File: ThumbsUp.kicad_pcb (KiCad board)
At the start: 2 copper layers, 251.1 x 336.1 mm, 135 parts, among them J1 Conn_01x04_Male, J10 Raiser_Male, J11 Raiser_Female, J12 Raiser_Male, J13 Raiser_Female, J14 Raiser_Male, J15 Raiser_Female, J16 Raiser_Male, J17 Raiser_Female, J18 Raiser_Male, J2 Conn_01x04_Male, J20 Conn_01x04_Female, J21 Conn_01x04_Female, J22 Conn_01x04_Female, J23 Conn_01x04_Female, J24 Conn_01x04_Male, J25 Conn_01x04_Male, J26 Conn_01x04_Male, J27 Conn_01x04_Male, J28 Conn_01x04_Female, J29 Conn_01x04_Female, J3 Conn_01x04_Female, J30 Conn_01x04_Female, J31 Conn_01x04_Female, J4 Conn_01x04_Male, J5 Conn_01x04_Female, J6 Conn_01x04_Male, J7 Conn_01x04_Male, J8 Conn_01x04_Male, J9 Raiser_Female, U1 ATmega32U4-AU, Y1 16MHz

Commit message: End of the day resuls
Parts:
- added J26: Conn_01x04_Male, Connector_PinHeader_2.54mm:PinHeader_1x04_P2.54mm_Vertical, F.Cu at (180.6, 164.0)
- added J27: Conn_01x04_Male, Connector_PinHeader_2.54mm:PinHeader_1x04_P2.54mm_Vertical, F.Cu at (187.1, 180.5)
- added J30: Conn_01x04_Female, Connector_PinSocket_2.54mm:PinSocket_1x04_P2.54mm_Vertical, F.Cu at (178.9, 301.4)
- added J31: Conn_01x04_Female, Connector_PinSocket_2.54mm:PinSocket_1x04_P2.54mm_Vertical, F.Cu at (185.4, 317.9)
- C1, C10, C2, C3, C4, C5, C6, C7, C8, C9, D1, D10, D11, D12, D13, D14, D15, D16, D17, D18, D19, D2, D20, D21, D22, D23, D24, D25, D26, D27, D28, D29, D3, D30, D31, D32, D33, D34, D35, D36, D37, D38, D39, D4, D40, D41, D42, D43, D44, D5, D6, D7, D8, D9, F1, R1, R2, R3, R4, U1, Y1: moved to B.Cu
- moved C5 38.6 mm to (177.7, -35.2)
- moved D14 33.1 mm to (179.0, 0.65)
- moved D20 33.1 mm to (173.3, 0.65)
- moved C9 32.7 mm to (177.7, -32.2)
- moved D12 30.7 mm to (192.4, -31.2)
- moved D23 29.0 mm to (37.9, -30.4)
- moved D24 29.0 mm to (49.4, -30.4)
- moved D25 29.0 mm to (55.1, -30.4)
- moved D32 29.0 mm to (124.1, -30.4)
- moved D33 29.0 mm to (118.4, -30.4)
- moved D34 29.0 mm to (112.6, -30.4)
- moved D35 29.0 mm to (106.9, -30.4)
- moved D36 29.0 mm to (101.1, -30.4)
- moved D37 29.0 mm to (43.6, -30.4)
- moved D38 29.0 mm to (95.4, -30.4)
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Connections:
- J10 pad 1: (no net) -> Net-(J10-Pad1)
- J10 pad 2: (no net) -> Net-(J10-Pad2)
- J10 pad 3: (no net) -> Net-(J10-Pad3)
- J10 pad 4: (no net) -> Net-(J10-Pad4)
- J11 pad 1: (no net) -> Net-(J11-Pad1)
- J11 pad 2: (no net) -> Net-(J11-Pad2)
- J11 pad 3: (no net) -> Net-(J11-Pad3)
- J11 pad 4: (no net) -> Net-(J11-Pad4)
- J13 pad 1: (no net) -> Net-(J13-Pad1)
- J13 pad 2: (no net) -> Net-(J13-Pad2)
- J13 pad 3: (no net) -> Net-(J13-Pad3)
- J13 pad 4: (no net) -> Net-(J13-Pad4)
- J14 pad 1: (no net) -> Net-(J14-Pad1)
- J14 pad 2: (no net) -> Net-(J14-Pad2)
- J14 pad 3: (no net) -> Net-(J14-Pad3)
- J14 pad 4: (no net) -> Net-(J14-Pad4)
- J15 pad 1: (no net) -> Net-(J15-Pad1)
- J15 pad 2: (no net) -> Net-(J15-Pad2)
- J15 pad 3: (no net) -> Net-(J15-Pad3)
- J15 pad 4: (no net) -> Net-(J15-Pad4)
- J17 pad 1: (no net) -> VCC
- J17 pad 2: (no net) -> SDA
- J17 pad 3: (no net) -> SCL
- J17 pad 4: (no net) -> GND
- J18 pad 1: (no net) -> VCC
- J18 pad 2: (no net) -> SDA
- J18 pad 3: (no net) -> SCL
- J18 pad 4: (no net) -> GND
- J20 pad 1: (no net) -> COL3
- J20 pad 2: (no net) -> COL2
- J20 pad 3: (no net) -> COL1
- J20 pad 4: (no net) -> COL0
- J21 pad 1: (no net) -> Net-(D4-Pad2)
- J21 pad 2: (no net) -> Net-(D3-Pad2)
- J21 pad 3: (no net) -> Net-(D2-Pad2)
- J21 pad 4: (no net) -> Net-(D1-Pad2)
- J22 pad 1: (no net) -> Net-(D8-Pad2)
- J22 pad 2: (no net) -> Net-(D7-Pad2)
- J22 pad 3: (no net) -> Net-(D6-Pad2)
- J22 pad 4: (no net) -> Net-(D5-Pad2)
- J23 pad 1: (no net) -> Net-(D12-Pad2)
- J23 pad 2: (no net) -> Net-(D11-Pad2)
- J23 pad 3: (no net) -> Net-(D10-Pad2)
- J23 pad 4: (no net) -> Net-(D9-Pad2)
- J24 pad 1: (no net) -> COL8
- J24 pad 2: (no net) -> COL9
- J24 pad 3: (no net) -> COLA
- J24 pad 4: (no net) -> COLB
- J25 pad 1: (no net) -> Net-(D34-Pad2)
- J25 pad 2: (no net) -> Net-(D33-Pad2)
- J25 pad 3: (no net) -> Net-(D32-Pad2)
- J25 pad 4: (no net) -> Net-(D31-Pad2)
- J26 pad 1: (no net) -> Net-(D38-Pad2)
- J26 pad 2: (no net) -> Net-(D37-Pad2)
- J26 pad 3: (no net) -> Net-(D36-Pad2)
- J26 pad 4: (no net) -> Net-(D35-Pad2)
- J27 pad 1: (no net) -> Net-(D42-Pad2)
- J27 pad 2: (no net) -> Net-(D41-Pad2)
- J27 pad 3: (no net) -> Net-(D40-Pad2)
- J27 pad 4: (no net) -> Net-(D39-Pad2)
- J3 pad 1: (no net) -> Net-(J3-Pad1)
- J3 pad 2: (no net) -> Net-(J3-Pad2)
- J3 pad 3: (no net) -> Net-(J3-Pad3)
- J3 pad 4: (no net) -> Net-(J3-Pad4)
- J4 pad 1: (no net) -> COL4
- J4 pad 2: (no net) -> Net-(D18-Pad2)
- J4 pad 3: (no net) -> Net-(D19-Pad2)
- J4 pad 4: (no net) -> COL5
- J5 pad 1: (no net) -> Net-(J5-Pad1)
- J5 pad 2: (no net) -> Net-(J5-Pad2)
- J5 pad 3: (no net) -> Net-(J5-Pad3)
- J5 pad 4: (no net) -> Net-(J5-Pad4)
- J6 pad 1: (no net) -> COL6
- J6 pad 2: (no net) -> Net-(D29-Pad2)
- J6 pad 3: (no net) -> Net-(D30-Pad2)
- J6 pad 4: (no net) -> COL7
- J9 pad 1: (no net) -> Net-(J9-Pad1)
- J9 pad 2: (no net) -> Net-(J9-Pad2)
- J9 pad 3: (no net) -> Net-(J9-Pad3)
- J9 pad 4: (no net) -> Net-(J9-Pad4)
- MX1 pad 1: Net-(MX1-Pad1) -> Net-(J1-Pad4)
- MX10 pad 1: (no net) -> COL2
- MX10 pad 2: (no net) -> Net-(D14-Pad2)
- MX11 pad 1: Net-(MX11-Pad1) -> Net-(J1-Pad1)
- MX12 pad 1: Net-(MX12-Pad1) -> Net-(J1-Pad1)
- MX14 pad 1: (no net) -> COL3
- MX14 pad 2: (no net) -> Net-(D13-Pad2)
- MX15 pad 1: (no net) -> Net-(MX15-Pad1)
- MX15 pad 2: (no net) -> Net-(D15-Pad2)
- MX16 pad 1: (no net) -> Net-(MX16-Pad1)
- MX16 pad 2: (no net) -> Net-(D16-Pad2)
- MX17 pad 1: (no net) -> Net-(MX17-Pad1)
- MX17 pad 2: (no net) -> Net-(D17-Pad2)
- MX18 pad 1: (no net) -> Net-(J3-Pad1)
- MX18 pad 2: (no net) -> Net-(J3-Pad2)
- MX19 pad 1: (no net) -> Net-(MX19-Pad1)
- MX19 pad 2: (no net) -> Net-(D20-Pad2)
- MX2 pad 1: Net-(MX2-Pad1) -> Net-(J1-Pad4)
- MX20 pad 1: (no net) -> Net-(MX20-Pad1)
- MX20 pad 2: (no net) -> Net-(D21-Pad2)
- MX21 pad 1: (no net) -> Net-(MX21-Pad1)
- MX21 pad 2: (no net) -> Net-(D22-Pad2)
- MX22 pad 1: (no net) -> Net-(J3-Pad4)
- MX22 pad 2: (no net) -> Net-(J3-Pad3)
- MX23 pad 1: (no net) -> Net-(MX23-Pad1)
- MX23 pad 2: (no net) -> Net-(D23-Pad2)
- MX24 pad 1: (no net) -> Net-(MX24-Pad1)
- MX24 pad 2: (no net) -> Net-(D24-Pad2)
- MX25 pad 1: (no net) -> Net-(MX25-Pad1)
- MX25 pad 2: (no net) -> Net-(D25-Pad2)
- MX26 pad 1: (no net) -> Net-(J5-Pad1)
- MX26 pad 2: (no net) -> Net-(J5-Pad2)
- MX27 pad 1: (no net) -> Net-(MX27-Pad1)
- MX27 pad 2: (no net) -> Net-(D26-Pad2)
- MX28 pad 1: (no net) -> Net-(MX28-Pad1)
- MX28 pad 2: (no net) -> Net-(D27-Pad2)
- MX29 pad 1: (no net) -> Net-(MX29-Pad1)
- MX29 pad 2: (no net) -> Net-(D28-Pad2)
- MX30 pad 1: (no net) -> Net-(J5-Pad4)
- MX30 pad 2: (no net) -> Net-(J5-Pad3)
- MX34 pad 1: (no net) -> COL8
- MX34 pad 2: (no net) -> Net-(D43-Pad2)
- MX38 pad 1: (no net) -> COL9
- MX38 pad 2: (no net) -> Net-(D44-Pad2)
- MX39 pad 1: Net-(MX39-Pad1) -> Net-(J28-Pad3)
- MX4 pad 1: Net-(MX4-Pad1) -> Net-(J1-Pad3)
- MX40 pad 1: Net-(MX40-Pad1) -> Net-(J28-Pad3)
- MX42 pad 1: Net-(MX42-Pad1) -> Net-(J28-Pad4)
- MX43 pad 1: Net-(MX43-Pad1) -> Net-(J28-Pad4)
- MX5 pad 1: Net-(MX5-Pad1) -> Net-(J1-Pad3)
- MX7 pad 1: Net-(MX7-Pad1) -> Net-(J1-Pad2)
- MX8 pad 1: Net-(MX8-Pad1) -> Net-(J1-Pad2)
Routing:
- net Net-(J28-Pad4): track 0.00 -> 123.3 mm
- net Net-(J1-Pad4): track 0.00 -> 119.0 mm, vias 0 -> 1
- net Net-(J28-Pad1): track 0.00 -> 109.6 mm, vias 0 -> 2
- net Net-(J8-Pad1): track 0.00 -> 108.3 mm
- net Net-(J7-Pad1): track 0.00 -> 107.5 mm
- net Net-(J1-Pad1): track 0.00 -> 106.8 mm
- net Net-(J30-Pad1): track 0.00 -> 104.9 mm
- net Net-(J1-Pad3): track 0.00 -> 104.5 mm, vias 0 -> 1
- net Net-(J29-Pad1): track 0.00 -> 100.3 mm
- net Net-(J28-Pad3): track 0.00 -> 97.1 mm, vias 0 -> 2
- net Net-(J1-Pad2): track 0.00 -> 96.2 mm
- net Net-(J31-Pad1): track 0.00 -> 96.2 mm
- net Net-(J2-Pad1): track 0.00 -> 94.8 mm
- net Net-(J28-Pad2): track 0.00 -> 90.4 mm, vias 0 -> 2
- net Net-(J2-Pad2): track 0.00 -> 82.4 mm
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
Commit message: End of the day resuls
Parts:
- moved U1 234.1 mm to (146.6, 220.0)
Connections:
- MX15 pad 1: Net-(MX15-Pad1) -> COL4
- MX16 pad 1: Net-(MX16-Pad1) -> COL4
- MX17 pad 1: Net-(MX17-Pad1) -> COL4
- MX19 pad 1: Net-(MX19-Pad1) -> COL5
- MX20 pad 1: Net-(MX20-Pad1) -> COL5
- MX21 pad 1: Net-(MX21-Pad1) -> COL5
- MX23 pad 1: Net-(MX23-Pad1) -> COL6
- MX24 pad 1: Net-(MX24-Pad1) -> COL6
- MX25 pad 1: Net-(MX25-Pad1) -> COL6
- MX27 pad 1: Net-(MX27-Pad1) -> COL7
- MX28 pad 1: Net-(MX28-Pad1) -> COL7
- MX29 pad 1: Net-(MX29-Pad1) -> COL7
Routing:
- net COL7: track 0.00 -> 62.8 mm, vias 0 -> 3
- net COL4: track 0.00 -> 61.7 mm, vias 0 -> 3
- net COL6: track 0.00 -> 60.6 mm, vias 0 -> 3
- net COL5: track 0.00 -> 59.2 mm, vias 0 -> 4
- net COL9: track 0.00 -> 13.2 mm, vias 0 -> 1
- net COL8: track 0.00 -> 12.9 mm, vias 0 -> 1
- net Net-(J1-Pad4): track 119.0 -> 130.2 mm
- net Net-(J29-Pad1): track 100.3 -> 110.0 mm
- net Net-(J30-Pad1): track 104.9 -> 112.9 mm
- net Net-(J28-Pad1): track 109.6 -> 115.7 mm
- net Net-(J29-Pad3): track 51.9 -> 57.8 mm
- net Net-(J28-Pad3): track 97.1 -> 102.7 mm
- net Net-(J8-Pad2): track 74.7 -> 80.3 mm
- net Net-(J28-Pad2): track 90.4 -> 95.0 mm
- net Net-(J8-Pad1): track 108.3 -> 104.5 mm
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
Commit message: Laid some tracks
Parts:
- added SW1: SW_Push, random-keyboard-parts:SKQG-1155865, B.Cu at (164.7, 227.9)
- added USB1: Molex-0548190589, random-keyboard-parts:Molex-0548190589, B.Cu at (146.7, 155.0)
- moved R4 275.0 mm to (158.8, 221.9), turned to 180 degrees
- moved D44 273.2 mm to (194.5, 208.0), turned to 90 degrees
- moved D43 269.4 mm to (192.1, 208.0), turned to 90 degrees
- moved D25 268.1 mm to (177.8, 208.0), turned to 90 degrees
- moved C9 262.9 mm to (128.0, 225.9)
- moved D42 261.6 mm to (180.2, 208.0), turned to 90 degrees
- moved D41 260.2 mm to (182.6, 208.0), turned to 90 degrees
- moved C6 259.0 mm to (131.5, 221.6)
- moved D40 258.9 mm to (184.9, 208.0), turned to 90 degrees
- moved D39 257.6 mm to (187.3, 208.0), turned to 90 degrees
- moved C10 254.2 mm to (124.8, 220.7)
- moved D12 251.2 mm to (115.9, 208.0), turned to 90 degrees
- moved C7 251.1 mm to (131.2, 216.0)
- moved C1 249.1 mm to (129.8, 218.8)
- moved D19 248.7 mm to (96.8, 208.0), turned to 90 degrees
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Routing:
- net Net-(D27-Pad2): track 0.00 -> 70.5 mm, vias 0 -> 1
- net Net-(D26-Pad2): track 0.00 -> 69.3 mm, vias 0 -> 1
- net Net-(D15-Pad2): track 0.00 -> 65.0 mm, vias 0 -> 1
- net Net-(D16-Pad2): track 0.00 -> 64.6 mm, vias 0 -> 1
- net Net-(D14-Pad2): track 0.00 -> 62.7 mm, vias 0 -> 2
- net COL5: track 59.2 -> 119.7 mm, vias 4 -> 1
- net Net-(D44-Pad2): track 0.00 -> 59.6 mm
- net COL6: track 60.6 -> 113.0 mm, vias 3 -> 2
- net Net-(D5-Pad2): track 0.00 -> 52.4 mm, vias 0 -> 1
- net Net-(D6-Pad2): track 0.00 -> 51.2 mm, vias 0 -> 1
- net COL7: track 62.8 -> 110.8 mm, vias 3 -> 1
- net Net-(J5-Pad3): track 0.00 -> 47.7 mm
- net Net-(D35-Pad2): track 0.00 -> 47.7 mm, vias 0 -> 1
- net Net-(D28-Pad2): track 0.00 -> 47.2 mm, vias 0 -> 1
- net COL3: track 0.00 -> 46.8 mm
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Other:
- net class Power added: clearance 0.2, trace_width 0.381, via_dia 0.8, via_drill 0.4

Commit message: Tracks are almost finished
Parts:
- moved C9 35.3 mm to (146.8, 196.1)
- moved C2 31.0 mm to (155.7, 207.8)
- moved C8 30.4 mm to (146.8, 199.2)
- moved C3 28.5 mm to (146.8, 201.6)
- moved C1 19.1 mm to (138.0, 201.6), turned to 180 degrees
- moved R4 18.3 mm to (140.5, 221.6), turned to 90 degrees
- moved C10 18.1 mm to (134.9, 205.6), turned to 270 degrees
- moved C7 17.4 mm to (147.6, 221.5), turned to 270 degrees
- moved C6 7.30 mm to (134.9, 215.1), turned to 90 degrees
- moved R3 6.95 mm to (151.6, 221.3)
- moved U1 5.18 mm to (144.5, 210.5)
- moved C4 2.86 mm to (165.9, 213.5)
- moved C5 2.86 mm to (165.9, 208.9)
- moved Y1 2.86 mm to (161.6, 211.3)
- moved F1 1.60 mm to (141.3, 188.9)
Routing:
- net ROW3: track 0.00 -> 126.8 mm
- net VCC: track 2.76 -> 118.6 mm, vias 0 -> 5
- net COLA: track 0.00 -> 115.8 mm, vias 0 -> 1
- net COLB: track 0.00 -> 115.4 mm, vias 0 -> 1
- net COL2: track 19.6 -> 125.6 mm, vias 1 -> 4
- net COL9: track 25.2 -> 130.8 mm, vias 0 -> 1
- net COL0: track 0.00 -> 104.7 mm, vias 0 -> 1
- net COL1: track 0.00 -> 104.6 mm, vias 0 -> 1
- net ROW2: track 2.32 -> 105.7 mm, vias 0 -> 2
- net COL8: track 45.6 -> 145.9 mm, vias 0 -> 1
- net COL7: track 110.8 -> 209.9 mm, vias 1 -> 3
- net COL3: track 46.8 -> 127.8 mm, vias 0 -> 3
- net GND: track 33.8 -> 114.3 mm, vias 0 -> 5
- net COL6: track 113.0 -> 177.7 mm, vias 2 -> 4
- net COL4: track 105.1 -> 168.7 mm, vias 0 -> 1
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- added copper zone on B.Cu, net GND

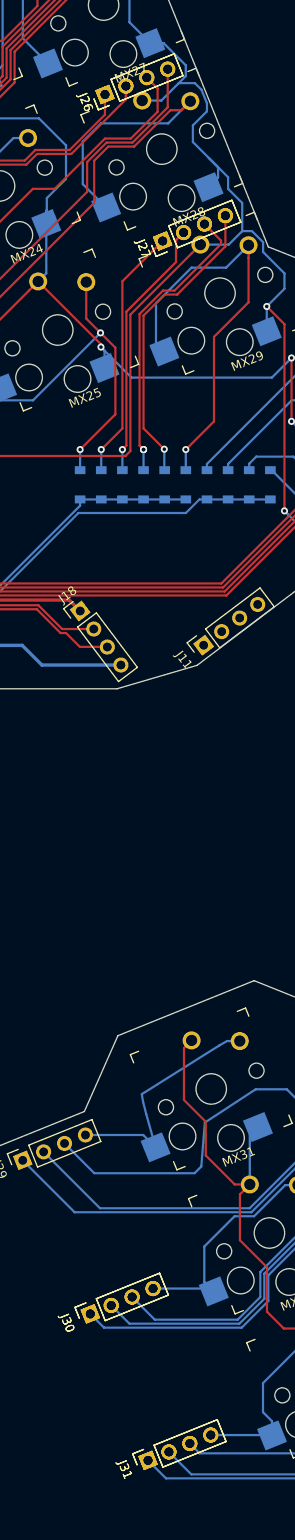
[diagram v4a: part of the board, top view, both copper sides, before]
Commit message: Removed the exta footprints
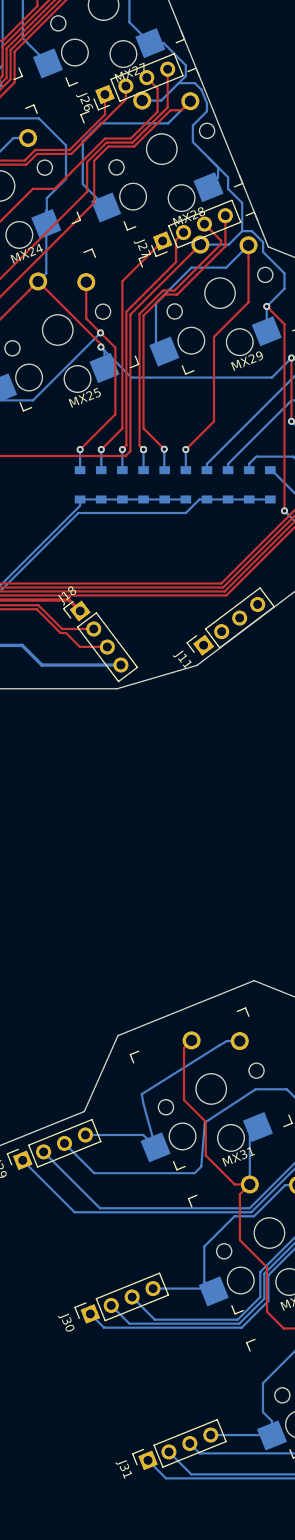
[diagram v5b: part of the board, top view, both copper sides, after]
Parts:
- removed the J26 at (180.6, 164.0)
- removed the J27 at (187.1, 180.5)
- removed the J30 at (178.9, 301.4)
- removed the J31 at (185.4, 317.9)
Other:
- board text added: "Thumbs Up! by Саша Карманов October 28, 2022 https://github.com/ak66666/ThumbsUpUnsplitV2"

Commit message: Somewhat completed the development
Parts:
- added G***: LOGO, Silkscreens:Crowfeet75, F.Cu at (148.6, 47.4)
- added G***: LOGO, Silkscreens:Crowfeet75, B.Cu at (143.6, 324.4)
- added J19: 52559-1233, 52559-1233:525591233, B.Cu at (150.3, 62.0)
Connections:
- J17 pad 2: SDA -> SDA-TOP
- J17 pad 3: SCL -> SCL-TOP
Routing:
- net GND: track 114.3 -> 198.2 mm, vias 5 -> 8
- net SCL-TOP: track 0.00 -> 61.4 mm
- net VCC: track 118.6 -> 178.7 mm
- net SDA-TOP: track 0.00 -> 59.8 mm
- net Net-(R3-Pad2): track 22.0 -> 40.7 mm, vias 2 -> 4
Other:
- board text added: "Thumbs Up! by Sasha Karmanov October 28, 2022 https://github.com/ak66666/ThumbsUpUnsplitV2"
- board text removed: "Thumbs Up! by Саша Карманов October 28, 2022 https://github.com/ak66666/ThumbsUpUnsplitV2"

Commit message: Moved the tracks from under MCU
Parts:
- removed G*** (x2): LOGO, Silkscreens:Crowfeet75
- moved C9 9.45 mm to (137.9, 199.2), turned to 180 degrees
- moved C10 1.49 mm to (133.7, 206.4)
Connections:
- C1 pad 1: VCC -> +5V
- C2 pad 1: VCC -> +5V
- C6 pad 1: VCC -> +5V
- C7 pad 1: VCC -> +5V
- F1 pad 1: VCC -> +5V
- F1 pad 2: +5V -> Net-(F1-Pad2)
- J17 pad 1: VCC -> +5V
- J18 pad 1: VCC -> +5V
- J19 pad 12: VCC -> +5V
- R3 pad 1: VCC -> +5V
- U1 pad 14: VCC -> +5V
- U1 pad 24: VCC -> +5V
- U1 pad 34: VCC -> +5V
- U1 pad 44: VCC -> +5V
- USB1 pad 5: +5V -> Net-(F1-Pad2)
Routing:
- net VCC: track 178.7 -> 0.00 mm, vias 5 -> 0
- net +5V: track 62.2 -> 196.7 mm, vias 3 -> 6
- net GND: track 198.2 -> 288.3 mm
- net Net-(F1-Pad2): track 0.00 -> 29.6 mm
- net (no net): track 13.7 -> 0.00 mm, vias 4 -> 0
- net COL3: track 127.8 -> 136.4 mm, vias 3 -> 2
- net Net-(R3-Pad2): track 40.7 -> 34.5 mm
- net COLB: track 115.4 -> 119.4 mm
- net COL9: track 130.8 -> 133.3 mm
- net COL5: track 150.3 -> 148.0 mm
- net COL6: track 177.7 -> 179.7 mm
- net COLA: track 115.8 -> 117.8 mm
- net COL8: track 145.9 -> 147.3 mm
- net Net-(C5-Pad1): track 17.6 -> 18.7 mm
- net Net-(C8-Pad1): track 6.52 -> 7.62 mm
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- removed copper zone on B.Cu, net GND

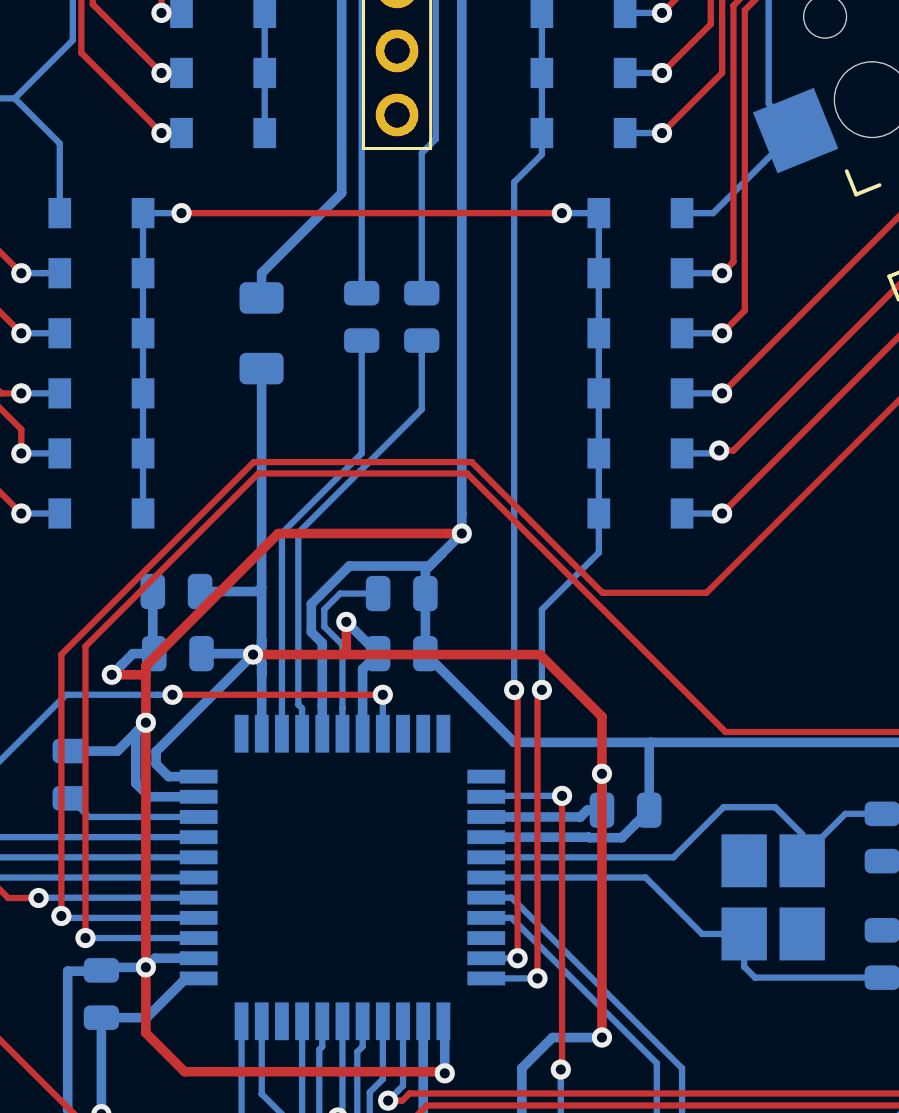
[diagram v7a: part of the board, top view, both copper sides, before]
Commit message: Moved the tracks from under MCU
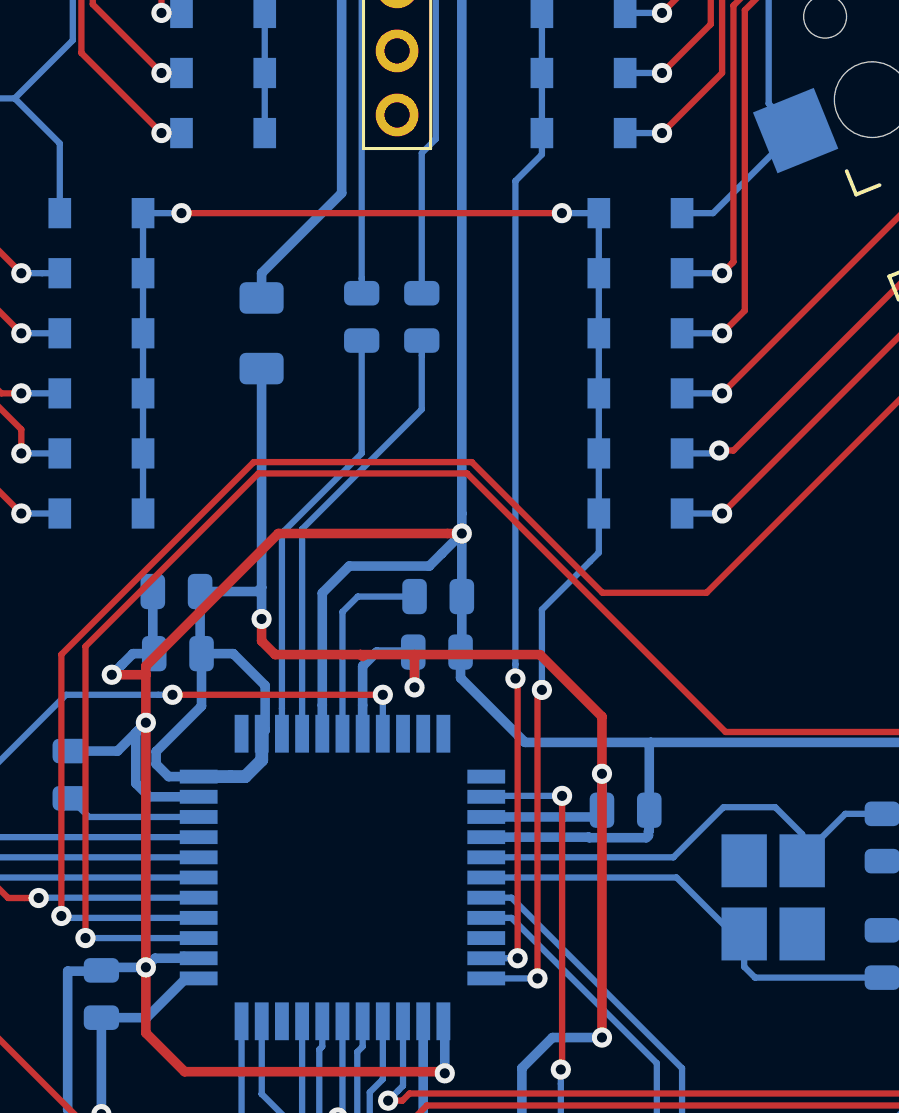
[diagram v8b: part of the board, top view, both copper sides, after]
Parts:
- moved C8 1.45 mm to (148.3, 199.3)
- moved C3 1.40 mm to (148.2, 201.6)
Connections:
- J17 pad 1: +5V -> VCC-TOP
- J17 pad 4: GND -> GND-TOP
- J19 pad 11: GND -> GND-TOP
- J19 pad 12: +5V -> VCC-TOP
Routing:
- net GND: track 288.3 -> 224.6 mm
- net GND-TOP: track 0.00 -> 63.6 mm
- net VCC-TOP: track 0.00 -> 59.5 mm
- net +5V: track 196.7 -> 143.0 mm
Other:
- net class Default: trace_width 0.25 -> 0.254
- net class Power: trace_width 0.381 -> 0.508
